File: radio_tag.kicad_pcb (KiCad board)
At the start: 4 copper layers, 60 x 24 mm, 20 parts, among them J1 Conn_01x01, J2 Conn_01x01, J3 Conn_01x01, J4 SMA, U1 TLV740P, U2 MICRF113, Y1 13M560

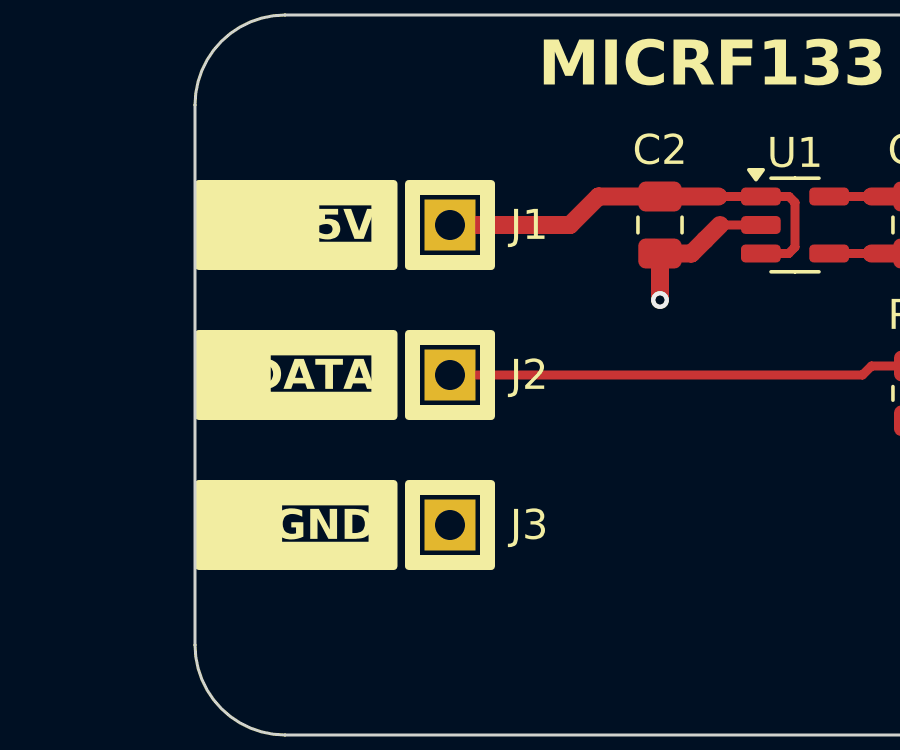
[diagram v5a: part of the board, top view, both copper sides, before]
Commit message: Add notes for dimensions and stackup
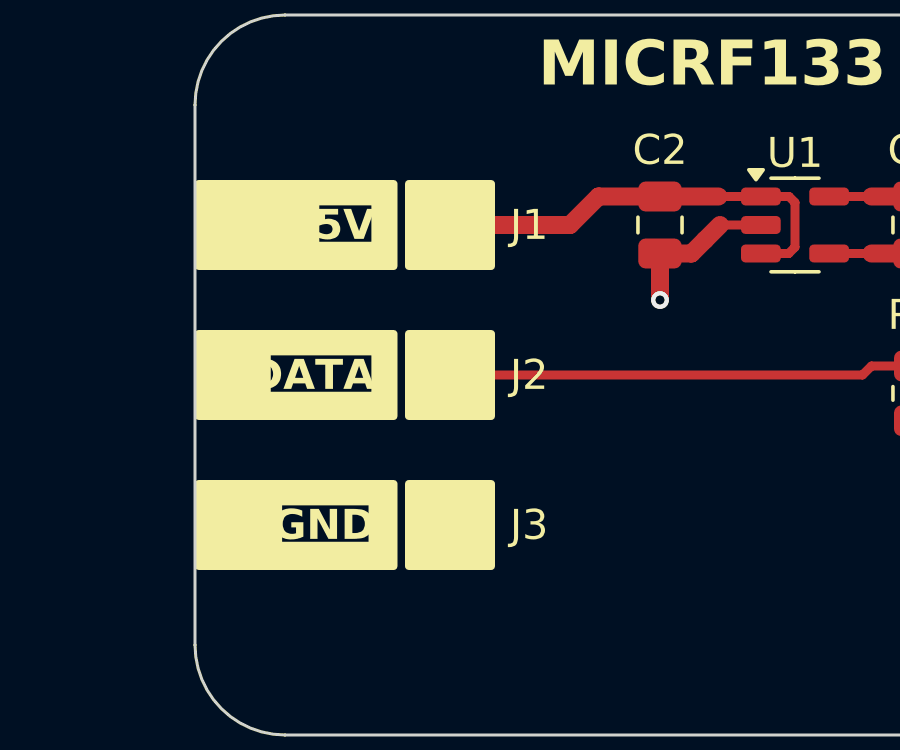
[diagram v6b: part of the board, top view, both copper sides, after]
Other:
- board text added: "Stackup: JLC04161H-7628"
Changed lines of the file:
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@@
 		(grid_origin 164 109.5)
 		(pcbplotparams
-			(layerselection 0x00010fc_ffffffff)
+			(layerselection 0x00013f0_ffffffff)
 			(plot_on_all_layers_selection 0x0000000_00000000)
 			(disableapertmacros no)
@@
 			(plotinvisibletext no)
 			(sketchpadsonfab no)
-			(subtractmaskfromsilk no)
+			(subtractmaskfromsilk yes)
 			(outputformat 1)
 			(mirror no)
-			(drillshape 1)
+			(drillshape 0)
 			(scaleselection 1)
-			(outputdirectory "")
+			(outputdirectory "out/gerbers")
 		)
 	)
@@
 	)
 	(gr_line
+		(start 234 109.5)
+		(end 234 101.5)
+		(stroke
+			(width 0.1)
+			(type default)
+		)
+		(layer "Dwgs.User")
+	)
+	(gr_line
+		(start 224 85.5)
+		(end 221 85.5)
+		(stroke
+			(width 0.1)
+			(type default)
+		)
+		(layer "Dwgs.User")
+	)
+	(gr_line
+		(start 164 109.5)
+		(end 164 106.5)
+		(stroke
+			(width 0.1)
+			(type default)
+		)
+		(layer "Dwgs.User")
+	)
+	(gr_line
+		(start 224 109.5)
+		(end 224 106.5)
+		(stroke
+			(width 0.1)
+			(type default)
+		)
+		(layer "Dwgs.User")
+	)
+	(gr_line
 		(start 167 85.5)
 		(end 221 85.5)
@@
 		)
 	)
+	(gr_text "Stackup:  JLC04161H-7628"
+		(at 165 118.5 0)
+		(layer "Cmts.User")
+		(effects
+			(font
+				(size 1 1)
+				(thickness 0.15)
+			)
+			(justify left bottom)
+		)
+	)
+	(dimension
+		(type aligned)
+		(layer "Dwgs.User")
+		(pts
+			(xy 164 109.5) (xy 224 109.5)
+		)
+		(height 2.999999)
+		(gr_text "60.0000 mm"
+			(at 194 111.349999 0)
+			(layer "Dwgs.User")
+			(effects
+				(font
+					(size 1 1)
+					(thickness 0.15)
+				)
+			)
+		)
+		(format
+			(prefix "")
+			(suffix "")
+			(units 3)
+			(units_format 1)
+			(precision 4)
+		)
+		(style
+			(thickness 0.1)
+			(arrow_length 1.27)
+			(text_position_mode 0)
+			(extension_height 0.58642)
+			(extension_offset 0.5) keep_text_aligned)
+	)
+	(dimension
+		(type aligned)
+		(layer "Dwgs.User")
+		(pts
+			(xy 164 109.5) (xy 234 109.5)
+		)
+		(height 5.999999)
+		(gr_text "70.0000 mm"
+			(at 199 114.349999 0)
+			(layer "Dwgs.User")
+			(effects
+				(font
+					(size 1 1)
+					(thickness 0.15)
+				)
+			)
+		)
+		(format
+			(prefix "")
+			(suffix "")
+			(units 3)
+			(units_format 1)
+			(precision 4)
+		)
+		(style
+			(thickness 0.1)
+			(arrow_length 1.27)
+			(text_position_mode 0)
+			(extension_height 0.58642)
+			(extension_offset 0.5) keep_text_aligned)
+	)
+	(dimension
+		(type aligned)
+		(layer "Dwgs.User")
+		(pts
+			(xy 224 109.5) (xy 224 85.5)
+		)
+		(height 16)
+		(gr_text "24.0000 mm"
+			(at 238.85 97.5 90)
+			(layer "Dwgs.User")
+			(effects
+				(font
+					(size 1 1)
+					(thickness 0.15)
+				)
+			)
+		)
+		(format
+			(prefix "")
+			(suffix "")
+			(units 3)
+			(units_format 1)
+			(precision 4)
+		)
+		(style
+			(thickness 0.1)
+			(arrow_length 1.27)
+			(text_position_mode 0)
+			(extension_height 0.58642)
+			(extension_offset 0.5) keep_text_aligned)
+	)
 	(segment
 		(start 179.5 93.45)
@@
 	)
 	(zone
-		(net 8)
-		(net_name "/PWR_TX_3V3")
+		(net 1)
+		(net_name "GND")
 		(layer "F.Cu")
 		(name "$teardrop_track$")
 		(hatch full 0.1)
-		(priority 30007)
+		(priority 30005)
 		(attr
 			(teardrop
@@
 		(polygon
 			(pts
-				(xy 185.95 91.4) (xy 185.95 91.7) (xy 186.435195 91.827164) (xy 186.551 91.55) (xy 186.435195 91.272836)
+				(xy 182.1 92.65) (xy 182.1 92.35) (xy 181.614805 92.222836) (xy 181.499 92.5) (xy 181.614805 92.777164)
 			)
 		)
 	)
 	(zone
-		(net 9)
-		(net_name "/PWR_IN")
+		(net 1)
+		(net_name "GND")
 		(layer "F.Cu")
-		(name "$teardrop_track$")
+		(name "$teardrop_padvia$")
 		(hatch full 0.1)
-		(priority 30008)
+		(priority 30004)
 		(attr
 			(teardrop
-				(type track_end)
+				(type padvia)
 			)
 		)
@@
 		(polygon
 			(pts
-				(xy 182.05 91.7) (xy 182.05 91.4) (xy 181.564805 91.272836) (xy 181.449 91.55) (xy 181.564805 91.827164)
+				(xy 188.15 99.9) (xy 187.85 99.9) (xy 187.722836 100.385195) (xy 188 100.501) (xy 188.277164 100.385195)
 			)
 		)
 	)
 	(zone
-		(net 1)
-		(net_name "GND")
+		(net 8)
+		(net_name "/PWR_TX_3V3")
 		(layer "F.Cu")
-		(name "$teardrop_padvia$")
+		(name "$teardrop_track$")
 		(hatch full 0.1)
-		(priority 30001)
+		(priority 30007)
 		(attr
 			(teardrop
-				(type padvia)
+				(type track_end)
 			)
 		)
@@
 		(polygon
 			(pts
-				(xy 219.6 94.84965) (xy 219.6 94.50035) (xy 219.114805 94.397836) (xy 218.999 94.675) (xy 219.114805 94.952164)
+				(xy 185.95 91.4) (xy 185.95 91.7) (xy 186.435195 91.827164) (xy 186.551 91.55) (xy 186.435195 91.272836)
 			)
 		)
@@
 		(net_name "GND")
 		(layer "F.Cu")
-		(name "$teardrop_padvia$")
+		(name "$teardrop_track$")
 		(hatch full 0.1)
-		(priority 30002)
+		(priority 30006)
 		(attr
 			(teardrop
-				(type padvia)
+				(type track_end)
 			)
 		)
@@
 		(polygon
 			(pts
-				(xy 213.17465 98.9) (xy 212.82535 98.9) (xy 212.722836 99.385195) (xy 213 99.501) (xy 213.277164 99.385195)
+				(xy 185.95 93.3) (xy 185.95 93.6) (xy 186.435195 93.727164) (xy 186.551 93.45) (xy 186.435195 93.172836)
 			)
 		)
@@
 		(net_name "GND")
 		(layer "F.Cu")
-		(name "$teardrop_track$")
+		(name "$teardrop_padvia$")
 		(hatch full 0.1)
-		(priority 30005)
+		(priority 30002)
 		(attr
 			(teardrop
-				(type track_end)
+				(type padvia)
 			)
 		)
@@
 		(polygon
 			(pts
-				(xy 182.1 92.65) (xy 182.1 92.35) (xy 181.614805 92.222836) (xy 181.499 92.5) (xy 181.614805 92.777164)
+				(xy 213.17465 98.9) (xy 212.82535 98.9) (xy 212.722836 99.385195) (xy 213 99.501) (xy 213.277164 99.385195)
 			)
 		)
@@
 		(net_name "GND")
 		(layer "F.Cu")
-		(name "$teardrop_track$")
+		(name "$teardrop_padvia$")
 		(hatch full 0.1)
-		(priority 30006)
+		(priority 30001)
 		(attr
 			(teardrop
-				(type track_end)
+				(type padvia)
 			)
 		)
@@
 		(polygon
 			(pts
-				(xy 185.95 93.3) (xy 185.95 93.6) (xy 186.435195 93.727164) (xy 186.551 93.45) (xy 186.435195 93.172836)
+				(xy 219.6 94.84965) (xy 219.6 94.50035) (xy 219.114805 94.397836) (xy 218.999 94.675) (xy 219.114805 94.952164)
 			)
 		)
 	)
 	(zone
-		(net 8)
-		(net_name "/PWR_TX_3V3")
+		(net 9)
+		(net_name "/PWR_IN")
 		(layer "F.Cu")
 		(name "$teardrop_track$")
 		(hatch full 0.1)
-		(priority 30003)
+		(priority 30008)
 		(attr
 			(teardrop
@@
 		(polygon
 			(pts
-				(xy 203.8 91.72465) (xy 203.8 91.37535) (xy 203.314805 91.272836) (xy 203.199 91.55) (xy 203.314805 91.827164)
+				(xy 182.05 91.7) (xy 182.05 91.4) (xy 181.564805 91.272836) (xy 181.449 91.55) (xy 181.564805 91.827164)
 			)
 		)
 	)
 	(zone
-		(net 1)
-		(net_name "GND")
+		(net 8)
+		(net_name "/PWR_TX_3V3")
 		(layer "F.Cu")
-		(name "$teardrop_padvia$")
+		(name "$teardrop_track$")
 		(hatch full 0.1)
-		(priority 30004)
+		(priority 30003)
 		(attr
 			(teardrop
-				(type padvia)
+				(type track_end)
 			)
 		)
@@
 		(polygon
 			(pts
-				(xy 188.15 99.9) (xy 187.85 99.9) (xy 187.722836 100.385195) (xy 188 100.501) (xy 188.277164 100.385195)
+				(xy 203.8 91.72465) (xy 203.8 91.37535) (xy 203.314805 91.272836) (xy 203.199 91.55) (xy 203.314805 91.827164)
 			)
 		)
@@
 		(layer "F.SilkS")
 		(hatch edge 0.5)
-		(connect_pads yes
-			(clearance 0)
-		)
-		(min_thickness 0.25)
-		(filled_areas_thickness no)
-		(keepout
-			(tracks allowed)
-			(vias allowed)
-			(pads allowed)
-			(copperpour not_allowed)
-			(footprints allowed)
-		)
-		(fill
-			(thermal_gap 0.5)
-			(thermal_bridge_width 0.5)
-		)
-		(polygon
-			(pts
-				(xy 171.5 91.5) (xy 173.5 91.5) (xy 173.5 93.5) (xy 171.5 93.5)
-			)
-		)
-	)
-	(zone
-		(net 0)
-		(net_name "")
-		(layer "F.SilkS")
-		(hatch edge 0.5)
 		(connect_pads
 			(clearance 0.5)
@@
 		(polygon
 			(pts
-				(xy 171.5 96.5) (xy 173.5 96.5) (xy 173.5 98.5) (xy 171.5 98.5)
-			)
-		)
-	)
-	(zone
-		(net 0)
-		(net_name "")
-		(layer "F.SilkS")
-		(hatch edge 0.5)
-		(connect_pads yes
-			(clearance 0)
-		)
-		(min_thickness 0.25)
-		(filled_areas_thickness no)
-		(keepout
-			(tracks allowed)
-			(vias allowed)
-			(pads allowed)
-			(copperpour not_allowed)
-			(footprints allowed)
-		)
-		(fill
-			(thermal_gap 0.5)
-			(thermal_bridge_width 0.5)
-		)
-		(polygon
-			(pts
 				(xy 171 101) (xy 170.75 101) (xy 170.75 104) (xy 171 104)
 			)
 		)
-	)
-	(zone
-		(net 0)
-		(net_name "")
-		(layer "F.SilkS")
-		(hatch edge 0.5)
-		(connect_pads yes
-			(clearance 0)
-		)
-		(min_thickness 0.25)
-		(filled_areas_thickness no)
-		(keepout
-			(tracks allowed)
-			(vias allowed)
-			(pads allowed)
-			(copperpour not_allowed)
-			(footprints allowed)
-		)
-		(fill
-			(thermal_gap 0.5)
-			(thermal_bridge_width 0.5)
-		)
-		(polygon
-			(pts
-				(xy 171.5 101.5) (xy 173.5 101.5) (xy 173.5 103.5) (xy 171.5 103.5)
-			)
-		)
